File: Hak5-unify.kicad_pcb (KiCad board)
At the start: 2 copper layers, 27.3 x 17.5 mm, 4 parts, among them J1 Conn_01x02, J2 Conn_01x03, U1 Unify-Nano

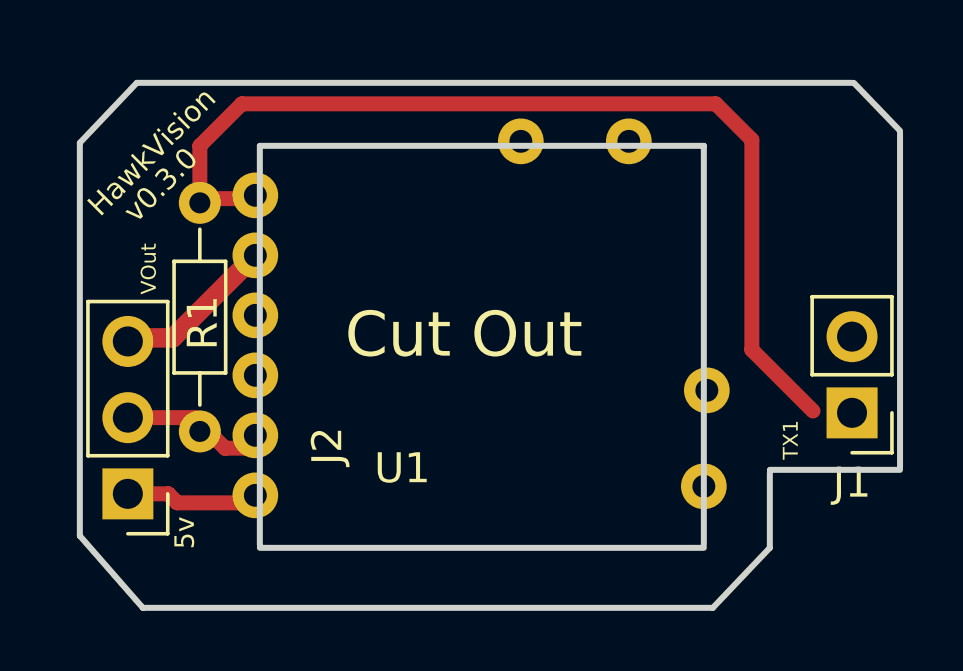
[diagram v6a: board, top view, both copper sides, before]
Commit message: fixes 2holes
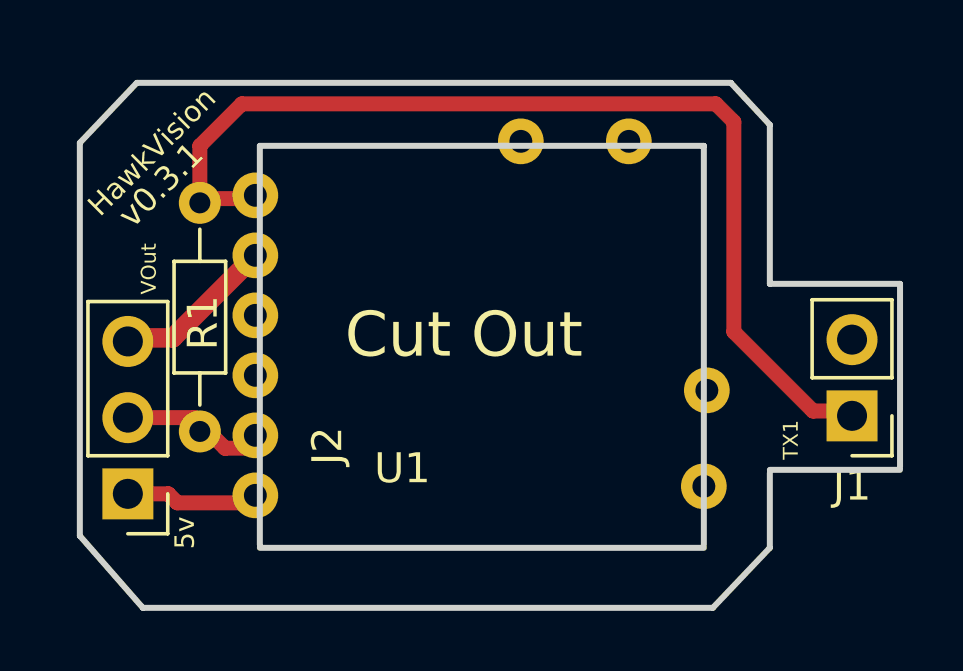
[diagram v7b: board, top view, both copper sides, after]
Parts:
- moved J1 0.10 mm to (125.7, 93.6)
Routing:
- net TX: track 33.1 -> 34.4 mm
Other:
- outline, holes or cut-outs redrawn
- board text added: "v0.3.1"
- board text removed: "v0.3.0"
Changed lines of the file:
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@@
   (general
     (thickness 1.6)
-    (drawings 21)
-    (tracks 16)
+    (drawings 23)
+    (tracks 18)
     (zones 0)
     (modules 4)
@@
   )
   (setup
-    (last_trace_width 0.25)
+    (last_trace_width 0.5)
     (user_trace_width 0.5)
     (user_trace_width 0.65)
@@
   )
   (module Pin_Headers:Pin_Header_Straight_1x02_Pitch2.54mm (layer F.Cu)
-    (at 125.74 93.5 180)
+    (at 125.74 93.6 180)
     (descr "Through hole straight pin header, 1x02, 2.54mm pitch, single row")
     (tags "Through hole pin header THT 1x02 2.54mm single row")
@@
     )
   )
+  (gr_line (start 121.7 82.5) (end 123 83.9) (layer Edge.Cuts) (width 0.2))
+  (gr_line (start 123 89.2) (end 123 83.9) (layer Edge.Cuts) (width 0.2))
+  (gr_line (start 127.34 89.2) (end 123 89.2) (layer Edge.Cuts) (width 0.2))
   (gr_line (start 123 98) (end 121.1 100) (layer Edge.Cuts) (width 0.2))
   (gr_text "Designed by Spencer in Utah" (at 113.45 98.95) (layer B.SilkS)
     (effects (font (size 0.65 0.65) (thickness 0.1625)) (justify mirror))
   )
-  (gr_line (start 125.8 82.5) (end 127.34 84.1) (layer Edge.Cuts) (width 0.2))
   (gr_line (start 100 84.5) (end 101.9 82.5) (layer Edge.Cuts) (width 0.2))
   (gr_line (start 100 97.6) (end 102.1 100) (layer Edge.Cuts) (width 0.2))
@@
     (effects (font (size 1.5 1.5) (thickness 0.3)))
   )
-  (gr_line (start 127.34 84.2) (end 127.34 95.3) (layer Edge.Cuts) (width 0.2))
+  (gr_line (start 127.34 89.2) (end 127.34 95.3) (layer Edge.Cuts) (width 0.2))
   (gr_line (start 100 84.5) (end 100 97.6) (layer Edge.Cuts) (width 0.2))
   (gr_line (start 102.1 100) (end 121.1 100) (layer Edge.Cuts) (width 0.2))
@@
     (effects (font (size 0.65 0.65) (thickness 0.1625)))
   )
-  (gr_text v0.3.0 (at 102.7 85.9 45) (layer F.SilkS)
-    (effects (font (size 0.7 0.7) (thickness 0.125)))
+  (gr_text v0.3.1 (at 102.7 85.9 45) (layer F.SilkS)
+    (effects (font (size 0.8 0.8) (thickness 0.125)))
   )
   (gr_text "HawkVision\n" (at 102.4 84.8 45) (layer F.SilkS)
     (effects (font (size 0.7 0.7) (thickness 0.125)))
   )
-  (gr_line (start 101.9 82.5) (end 125.74 82.5) (layer Edge.Cuts) (width 0.2))
+  (gr_line (start 101.9 82.5) (end 121.7 82.5) (layer Edge.Cuts) (width 0.2))
   (gr_line (start 106 98) (end 120.8 98) (layer Edge.Cuts) (width 0.2))
   (gr_line (start 106 84.6) (end 106 97.9) (layer Edge.Cuts) (width 0.2))
@@
   (segment (start 104.14 86.36) (end 105.94999 86.36) (width 0.5) (layer F.Cu) (net 5))
   (segment (start 104 84.6) (end 104 86.5) (width 0.5) (layer F.Cu) (net 5))
-  (segment (start 122.4 84.4) (end 121.2 83.2) (width 0.5) (layer F.Cu) (net 5))
   (segment (start 105.4 83.2) (end 104 84.6) (width 0.5) (layer F.Cu) (net 5))
   (segment (start 121.2 83.2) (end 105.4 83.2) (width 0.5) (layer F.Cu) (net 5))
-  (segment (start 122.4 91.4) (end 122.4 84.4) (width 0.5) (layer F.Cu) (net 5))
-  (segment (start 124.439999 93.439999) (end 122.4 91.4) (width 0.5) (layer F.Cu) (net 5))
+  (segment (start 121.8 90.8) (end 121.8 83.8) (width 0.5) (layer F.Cu) (net 5))
+  (segment (start 124.439999 93.439999) (end 121.8 90.8) (width 0.5) (layer F.Cu) (net 5))
+  (segment (start 125.579999 93.439999) (end 124.439999 93.439999) (width 0.5) (layer F.Cu) (net 5))
+  (segment (start 125.74 93.6) (end 125.579999 93.439999) (width 0.5) (layer F.Cu) (net 5))
+  (segment (start 121.8 83.8) (end 121.2 83.2) (width 0.5) (layer F.Cu) (net 5))
   (segment (start 103.1 91) (end 105.87499 88.22501) (width 0.65) (layer F.Cu) (net 8))
   (segment (start 101.6 91) (end 103.1 91) (width 0.65) (layer F.Cu) (net 8))

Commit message: v0.4.0
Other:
- outline, holes or cut-outs redrawn
- board text added: "v0.4.0"
- board text removed: "v0.3.1"
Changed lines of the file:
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@@
   )
   (setup
-    (last_trace_width 0.5)
+    (last_trace_width 0.25)
     (user_trace_width 0.5)
     (user_trace_width 0.65)
@@
     (descr "Through hole straight pin header, 1x02, 2.54mm pitch, single row")
     (tags "Through hole pin header THT 1x02 2.54mm single row")
-    (fp_text reference J1 (at 0 -2.33 180) (layer F.SilkS)
+    (fp_text reference J1 (at 7.04 -1.5 180) (layer F.SilkS)
       (effects (font (size 1 1) (thickness 0.15)))
     )
@@
   (gr_line (start 100 84.5) (end 101.9 82.5) (layer Edge.Cuts) (width 0.2))
   (gr_line (start 100 97.6) (end 102.1 100) (layer Edge.Cuts) (width 0.2))
-  (gr_line (start 123 95.5) (end 123 98) (layer Edge.Cuts) (width 0.2))
-  (gr_line (start 127.34 95.4) (end 123 95.4) (layer Edge.Cuts) (width 0.2))
+  (gr_line (start 123 95.2) (end 123 97.9) (layer Edge.Cuts) (width 0.2))
+  (gr_line (start 127.34 95.1) (end 123 95.1) (layer Edge.Cuts) (width 0.2))
   (gr_text "Cut Out" (at 112.8 90.9) (layer F.SilkS)
     (effects (font (size 1.5 1.5) (thickness 0.3)))
   )
-  (gr_line (start 127.34 89.2) (end 127.34 95.3) (layer Edge.Cuts) (width 0.2))
+  (gr_line (start 127.34 89.2) (end 127.34 95.1) (layer Edge.Cuts) (width 0.2))
   (gr_line (start 100 84.5) (end 100 97.6) (layer Edge.Cuts) (width 0.2))
   (gr_line (start 102.1 100) (end 121.1 100) (layer Edge.Cuts) (width 0.2))
-  (gr_text TX1 (at 123.7 94.4 90) (layer F.SilkS)
+  (gr_text TX1 (at 123.4 94 90) (layer F.SilkS)
     (effects (font (size 0.5 0.5) (thickness 0.125)))
   )
@@
     (effects (font (size 0.65 0.65) (thickness 0.1625)))
   )
-  (gr_text v0.3.1 (at 102.7 85.9 45) (layer F.SilkS)
+  (gr_text "v0.4.0\n" (at 102.7 85.9 45) (layer F.SilkS)
     (effects (font (size 0.8 0.8) (thickness 0.125)))
   )
